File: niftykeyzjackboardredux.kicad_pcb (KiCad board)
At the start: 2 copper layers, 90 x 29.1 mm, 6 parts

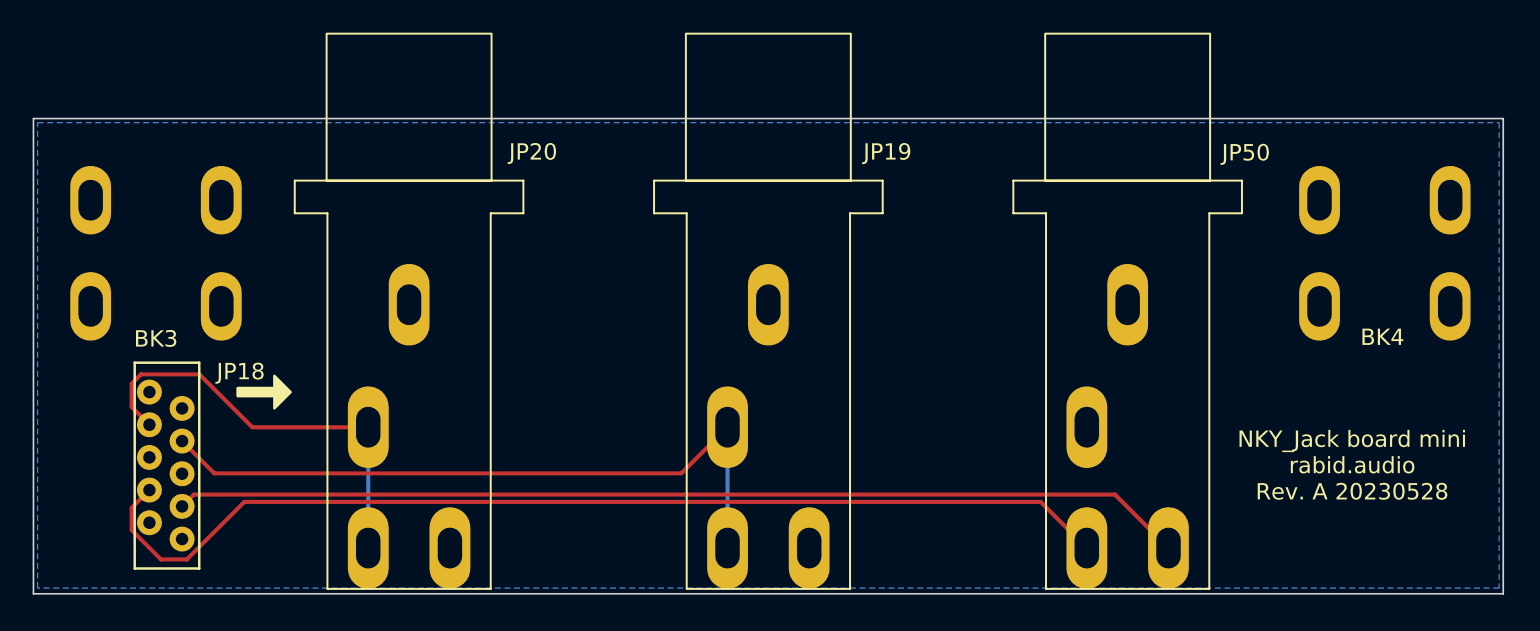
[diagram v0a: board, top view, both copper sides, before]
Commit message: adusted stick-out length
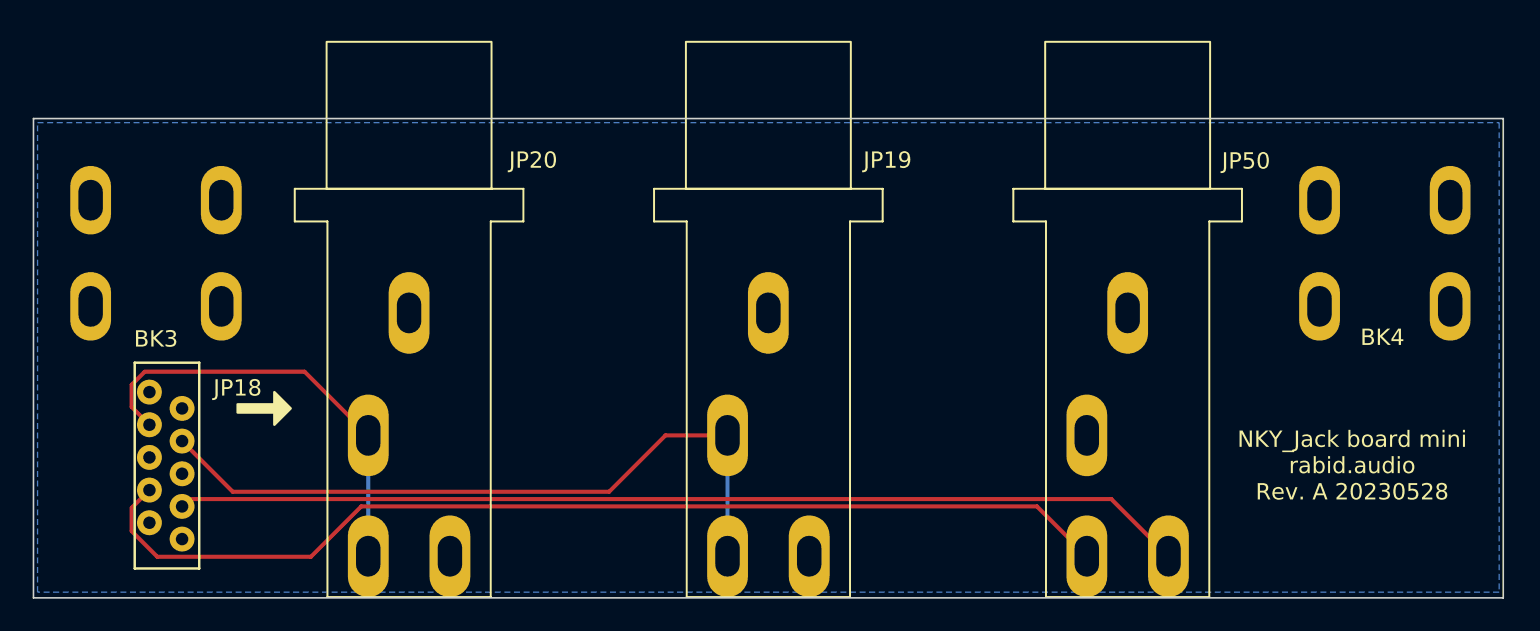
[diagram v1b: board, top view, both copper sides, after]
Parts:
- moved JP19 0.50 mm to (95.0, 67.0)
- moved JP20 0.50 mm to (73.0, 67.0)
- moved JP50 0.50 mm to (117.0, 67.0)
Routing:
- net Net-(JP19-PadT): track 42.8 -> 43.5 mm
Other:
- board size 90 x 29.1 mm -> 90 x 29.3 mm
- board text added: "(54.5-(3*10.6))/2 = 11.35 (54.5-10.6)/2=21.95 pushed jacks out extra 3.5mm from original"
- board text removed: "(54.5-(3*10.6))/2 = 11.35 (54.5-10.6)/2=21.95 pushed jacks out extra 4mm from original"
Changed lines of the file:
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@@
   )
   (footprint "components:Jack 6.35mm PJ603" locked (layer "F.Cu")
-    (at 117 66.5 -90)
+    (at 117 67 -90)
     (property "Sheetfile" "niftykeyzjackboardredux.kicad_sch")
     (property "Sheetname" "")
@@
       (effects (font (size 1 1) (thickness 0.15)))
     )
-    (fp_text value "HEADPHONES" (at -2.8 -3.5 -90) (layer "F.Fab")
+    (fp_text value "HEADPHONES" (at -2.8 -3.5 90) (layer "F.Fab")
       (effects (font (size 1 1) (thickness 0.15)))
     )
@@
   )
   (footprint "components:Jack 6.35mm PJ603" locked (layer "F.Cu")
-    (at 73 66.5 -90)
+    (at 73 67 -90)
     (property "Sheetfile" "niftykeyzjackboardredux.kicad_sch")
     (property "Sheetname" "")
@@
       (effects (font (size 1 1) (thickness 0.15)))
     )
-    (fp_text value "OUT1" (at -2.8 -3.5 -90) (layer "F.Fab")
+    (fp_text value "OUT1" (at -2.8 -3.5 90) (layer "F.Fab")
       (effects (font (size 1 1) (thickness 0.15)))
     )
@@
     (property "Sheetname" "")
     (attr through_hole)
-    (fp_text reference "JP18" (at 5.6 -1.25 unlocked) (layer "F.SilkS")
+    (fp_text reference "JP18" (at 5.4 -0.25 unlocked) (layer "F.SilkS")
       (effects (font (size 1 1) (thickness 0.15)))
     )
@@
       (effects (font (size 1 1) (thickness 0.15)))
     )
-    (fp_text user "${REFERENCE}" (at 5.6 -1.25 unlocked) (layer "F.Fab")
+    (fp_text user "${REFERENCE}" (at 5.4 -0.25 unlocked) (layer "F.Fab")
       (effects (font (size 1 1) (thickness 0.15)))
     )
@@
   )
   (footprint "components:Jack 6.35mm PJ603" locked (layer "F.Cu")
-    (at 95 66.5 -90)
+    (at 95 67 -90)
     (property "Sheetfile" "niftykeyzjackboardredux.kicad_sch")
     (property "Sheetname" "")
@@
       (effects (font (size 1 1) (thickness 0.15)))
     )
-    (fp_text value "OUT2" (at -2.8 -3.5 -90) (layer "F.Fab")
+    (fp_text value "OUT2" (at -2.8 -3.5 90) (layer "F.Fab")
       (effects (font (size 1 1) (thickness 0.15)))
     )
@@
   (gr_poly
     (pts
-      (xy 65.75 66.75)
-      (xy 64.75 67.75)
-      (xy 64.75 67)
-      (xy 62.5 67)
-      (xy 62.5 66.5)
-      (xy 64.75 66.5)
-      (xy 64.75 65.75)
+      (xy 65.75 67.75)
+      (xy 64.75 68.75)
+      (xy 64.75 68)
+      (xy 62.5 68)
+      (xy 62.5 67.5)
+      (xy 64.75 67.5)
+      (xy 64.75 66.75)
     ) (layer "F.SilkS") (width 0.15) (fill solid))
-  (gr_rect (start 50 50) (end 140 79.1) (layer "Edge.Cuts") (width 0.1) (fill none))
+  (gr_rect (start 50 50) (end 140 79.35) (layer "Edge.Cuts") (width 0.1) (fill none))
   (gr_text "NKY_Jack board mini\nrabid.audio\nRev. A 20230528" (at 130.75 71.25) (layer "F.SilkS")
     (effects (font (size 1 1) (thickness 0.15)))
   )
-  (gr_text "(54.5-(3*10.6))/2 = 11.35\n(54.5-10.6)/2=21.95\npushed jacks out extra 4mm from original" (at 80 38.75) (layer "F.Fab")
+  (gr_text "(54.5-(3*10.6))/2 = 11.35\n(54.5-10.6)/2=21.95\npushed jacks out extra 3.5mm from original" (at 80 38.75) (layer "F.Fab")
     (effects (font (size 1 1) (thickness 0.15)))
   )
-  (segment (start 59.825 73.025) (end 59.1 73.75) (width 0.25) (layer "F.Cu") (net 2))
-  (segment (start 116.225 73.025) (end 59.825 73.025) (width 0.25) (layer "F.Cu") (net 2))
-  (segment (start 119.5 76.3) (end 116.225 73.025) (width 0.25) (layer "F.Cu") (net 2))
-  (segment (start 60.163 65.663) (end 63.4 68.9) (width 0.25) (layer "F.Cu") (net 3))
-  (segment (start 56.013 67.663) (end 56.013 66.237) (width 0.25) (layer "F.Cu") (net 3))
+  (segment (start 119.5 76.8) (end 116 73.3) (width 0.25) (layer "F.Cu") (net 2))
+  (segment (start 116 73.3) (end 59.55 73.3) (width 0.25) (layer "F.Cu") (net 2))
+  (segment (start 59.55 73.3) (end 59.1 73.75) (width 0.25) (layer "F.Cu") (net 2))
+  (segment (start 56.013 66.299749) (end 56.812749 65.5) (width 0.25) (layer "F.Cu") (net 3))
+  (segment (start 56.013 67.663) (end 56.013 66.299749) (width 0.25) (layer "F.Cu") (net 3))
+  (segment (start 66.6 65.5) (end 70.5 69.4) (width 0.25) (layer "F.Cu") (net 3))
   (segment (start 57.1 68.75) (end 56.013 67.663) (width 0.25) (layer "F.Cu") (net 3))
-  (segment (start 56.013 66.237) (end 56.587 65.663) (width 0.25) (layer "F.Cu") (net 3))
-  (segment (start 56.587 65.663) (end 60.163 65.663) (width 0.25) (layer "F.Cu") (net 3))
-  (segment (start 63.4 68.9) (end 70.5 68.9) (width 0.25) (layer "F.Cu") (net 3))
-  (segment (start 70.5 68.9) (end 70.5 76.3) (width 0.25) (layer "B.Cu") (net 3))
-  (segment (start 89.675 71.725) (end 92.5 68.9) (width 0.25) (layer "F.Cu") (net 4))
-  (segment (start 59.1 69.75) (end 61.075 71.725) (width 0.25) (layer "F.Cu") (net 4))
-  (segment (start 61.075 71.725) (end 89.675 71.725) (width 0.25) (layer "F.Cu") (net 4))
-  (segment (start 92.5 68.9) (end 92.5 76.3) (width 0.25) (layer "B.Cu") (net 4))
-  (segment (start 56.013 73.837) (end 57.1 72.75) (width 0.25) (layer "F.Cu") (net 5))
-  (segment (start 62.912251 73.475) (end 59.387251 77) (width 0.25) (layer "F.Cu") (net 5))
-  (segment (start 57.812749 77) (end 56.013 75.200251) (width 0.25) (layer "F.Cu") (net 5))
-  (segment (start 59.387251 77) (end 57.812749 77) (width 0.25) (layer "F.Cu") (net 5))
-  (segment (start 111.675 73.475) (end 62.912251 73.475) (width 0.25) (layer "F.Cu") (net 5))
-  (segment (start 56.013 75.200251) (end 56.013 73.837) (width 0.25) (layer "F.Cu") (net 5))
-  (segment (start 114.5 76.3) (end 111.675 73.475) (width 0.25) (layer "F.Cu") (net 5))
+  (segment (start 56.812749 65.5) (end 66.6 65.5) (width 0.25) (layer "F.Cu") (net 3))
+  (segment (start 70.5 69.4) (end 70.5 76.8) (width 0.25) (layer "B.Cu") (net 3))
+  (segment (start 85.25 72.85) (end 88.7 69.4) (width 0.25) (layer "F.Cu") (net 4))
+  (segment (start 62.2 72.85) (end 85.25 72.85) (width 0.25) (layer "F.Cu") (net 4))
+  (segment (start 59.1 69.75) (end 62.2 72.85) (width 0.25) (layer "F.Cu") (net 4))
+  (segment (start 88.7 69.4) (end 92.5 69.4) (width 0.25) (layer "F.Cu") (net 4))
+  (segment (start 92.5 76.8) (end 92.5 69.4) (width 0.25) (layer "B.Cu") (net 4))
+  (segment (start 57.1 72.75) (end 56.013 73.837) (width 0.25) (layer "F.Cu") (net 5))
+  (segment (start 56.013 75.263) (end 57.587 76.837) (width 0.25) (layer "F.Cu") (net 5))
+  (segment (start 56.013 73.837) (end 56.013 75.263) (width 0.25) (layer "F.Cu") (net 5))
+  (segment (start 57.587 76.837) (end 66.985614 76.837) (width 0.25) (layer "F.Cu") (net 5))
+  (segment (start 70.072614 73.75) (end 111.45 73.75) (width 0.25) (layer "F.Cu") (net 5))
+  (segment (start 66.985614 76.837) (end 70.072614 73.75) (width 0.25) (layer "F.Cu") (net 5))
+  (segment (start 111.45 73.75) (end 114.5 76.8) (width 0.25) (layer "F.Cu") (net 5))
   (zone (net 1) (net_name "GND") (layer "B.Cu") (hatch edge 0.508)
     (connect_pads (clearance 0.508))
@@
     (polygon
       (pts
-        (xy 139.75 78.75)
-        (xy 50.25 78.75)
+        (xy 139.75 79)
+        (xy 50.25 79)
         (xy 50.25 50.25)
         (xy 139.75 50.25)
@@
     )
   )
+  (group "" locked (id 65ac9146-4b58-4e47-bd66-f6dcea7674e5)
+    (members
+      6b817d68-1e01-4d03-8519-fe86ffb6e69e
+      ba459322-174a-4526-8520-4337cc23d4d2
+      d0c782eb-eb72-43f2-9ef1-8a42a7ce99fa
+    )
+  )

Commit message: update board
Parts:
- moved BK3 0.64 mm to (53.5, 54.4)
- moved BK4 0.61 mm to (128.8, 54.4)
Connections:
- JP18 pad 3: Net-(JP20-PadT) -> Net-(JP18-Pad3)
- JP18 pad 4: Net-(JP19-PadT) -> Net-(JP18-Pad4)
- JP19 pad T: Net-(JP19-PadT) -> Net-(JP18-Pad4)
- JP19 pad TN: Net-(JP19-PadT) -> unconnected-(JP19-PadTN)
- JP20 pad T: Net-(JP20-PadT) -> Net-(JP18-Pad3)
- JP20 pad TN: Net-(JP20-PadT) -> unconnected-(JP20-PadTN)
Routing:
- net Net-(JP19-PadT): track 43.5 -> 0.00 mm
- net Net-(JP18-Pad4): track 0.00 -> 37.4 mm, vias 0 -> 1
- net Net-(JP20-PadT): track 26.7 -> 0.00 mm
- net Net-(JP18-Pad3): track 0.00 -> 23.4 mm
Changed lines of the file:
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@@
   (net 1 "GND")
   (net 2 "Net-(JP18-Pad8)")
-  (net 3 "Net-(JP20-PadT)")
-  (net 4 "Net-(JP19-PadT)")
-  (net 5 "Net-(JP50-PadT)")
+  (net 3 "Net-(JP18-Pad3)")
+  (net 4 "Net-(JP18-Pad4)")
+  (net 5 "Net-(JP18-Pad7)")
   (net 6 "unconnected-(JP50-PadTN)")
+  (net 7 "unconnected-(JP19-PadTN)")
+  (net 8 "unconnected-(JP20-PadTN)")
   (footprint "components:screw-mount" locked (layer "F.Cu")
-    (at 128.75 55)
+    (at 128.75 54.388)
     (property "Sheetfile" "niftykeyzjackboardredux.kicad_sch")
     (property "Sheetname" "")
@@
       (net 2 "Net-(JP18-Pad8)") (pintype "passive"))
     (pad "T" thru_hole oval locked (at 9.8 2.5 270) (size 5 2.5) (drill oval 2.5 1.5) (layers *.Cu *.Mask)
-      (net 5 "Net-(JP50-PadT)") (pintype "passive"))
+      (net 5 "Net-(JP18-Pad7)") (pintype "passive"))
     (pad "TN" thru_hole oval locked (at 2.4 2.5 270) (size 5 2.5) (drill oval 2.5 1.5) (layers *.Cu *.Mask)
       (net 6 "unconnected-(JP50-PadTN)") (pintype "passive+no_connect"))
   )
   (footprint "components:screw-mount" locked (layer "F.Cu")
-    (at 53.5 55)
+    (at 53.5 54.356)
     (property "Sheetfile" "niftykeyzjackboardredux.kicad_sch")
     (property "Sheetname" "")
@@
       (net 1 "GND") (pintype "passive"))
     (pad "T" thru_hole oval locked (at 9.8 2.5 270) (size 5 2.5) (drill oval 2.5 1.5) (layers *.Cu *.Mask)
-      (net 3 "Net-(JP20-PadT)") (pintype "passive"))
+      (net 3 "Net-(JP18-Pad3)") (pintype "passive"))
     (pad "TN" thru_hole oval locked (at 2.4 2.5 270) (size 5 2.5) (drill oval 2.5 1.5) (layers *.Cu *.Mask)
-      (net 3 "Net-(JP20-PadT)") (pintype "passive"))
+      (net 8 "unconnected-(JP20-PadTN)") (pintype "passive+no_connect"))
   )
   (footprint "components:HLW10S-2C7LF" (layer "F.Cu")
@@
       (net 1 "GND") (pinfunction "Pin_2") (pintype "passive"))
     (pad "3" thru_hole circle (at 0 2) (size 1.524 1.524) (drill 0.762) (layers *.Cu *.Mask)
-      (net 3 "Net-(JP20-PadT)") (pinfunction "Pin_3") (pintype "passive"))
+      (net 3 "Net-(JP18-Pad3)") (pinfunction "Pin_3") (pintype "passive"))
     (pad "4" thru_hole circle (at 2 3) (size 1.524 1.524) (drill 0.762) (layers *.Cu *.Mask)
-      (net 4 "Net-(JP19-PadT)") (pinfunction "Pin_4") (pintype "passive"))
+      (net 4 "Net-(JP18-Pad4)") (pinfunction "Pin_4") (pintype "passive"))
     (pad "5" thru_hole circle (at 0 4) (size 1.524 1.524) (drill 0.762) (layers *.Cu *.Mask)
       (net 1 "GND") (pinfunction "Pin_5") (pintype "passive"))
@@
       (net 1 "GND") (pinfunction "Pin_6") (pintype "passive"))
     (pad "7" thru_hole circle (at 0 6) (size 1.524 1.524) (drill 0.762) (layers *.Cu *.Mask)
-      (net 5 "Net-(JP50-PadT)") (pinfunction "Pin_7") (pintype "passive"))
+      (net 5 "Net-(JP18-Pad7)") (pinfunction "Pin_7") (pintype "passive"))
     (pad "8" thru_hole circle (at 2 7) (size 1.524 1.524) (drill 0.762) (layers *.Cu *.Mask)
       (net 2 "Net-(JP18-Pad8)") (pinfunction "Pin_8") (pintype "passive"))
@@
       (net 1 "GND") (pintype "passive"))
     (pad "T" thru_hole oval locked (at 9.8 2.5 270) (size 5 2.5) (drill oval 2.5 1.5) (layers *.Cu *.Mask)
-      (net 4 "Net-(JP19-PadT)") (pintype "passive"))
+      (net 4 "Net-(JP18-Pad4)") (pintype "passive"))
     (pad "TN" thru_hole oval locked (at 2.4 2.5 270) (size 5 2.5) (drill oval 2.5 1.5) (layers *.Cu *.Mask)
-      (net 4 "Net-(JP19-PadT)") (pintype "passive"))
+      (net 7 "unconnected-(JP19-PadTN)") (pintype "passive+no_connect"))
   )
   (gr_rect (start 60.15 64.95) (end 56.2 77.55) (layer "F.SilkS") (width 0.15) (fill none))
@@
   (segment (start 116 73.3) (end 59.55 73.3) (width 0.25) (layer "F.Cu") (net 2))
   (segment (start 59.55 73.3) (end 59.1 73.75) (width 0.25) (layer "F.Cu") (net 2))
-  (segment (start 56.013 66.299749) (end 56.812749 65.5) (width 0.25) (layer "F.Cu") (net 3))
-  (segment (start 56.013 67.663) (end 56.013 66.299749) (width 0.25) (layer "F.Cu") (net 3))
-  (segment (start 66.6 65.5) (end 70.5 69.4) (width 0.25) (layer "F.Cu") (net 3))
-  (segment (start 57.1 68.75) (end 56.013 67.663) (width 0.25) (layer "F.Cu") (net 3))
-  (segment (start 56.812749 65.5) (end 66.6 65.5) (width 0.25) (layer "F.Cu") (net 3))
-  (segment (start 70.5 69.4) (end 70.5 76.8) (width 0.25) (layer "B.Cu") (net 3))
-  (segment (start 85.25 72.85) (end 88.7 69.4) (width 0.25) (layer "F.Cu") (net 4))
+  (segment (start 55.563 70.287) (end 55.563 75.449396) (width 0.25) (layer "F.Cu") (net 3))
+  (segment (start 69.83 77.47) (end 70.5 76.8) (width 0.25) (layer "F.Cu") (net 3))
+  (segment (start 55.563 75.449396) (end 57.583604 77.47) (width 0.25) (layer "F.Cu") (net 3))
+  (segment (start 57.1 68.75) (end 55.563 70.287) (width 0.25) (layer "F.Cu") (net 3))
+  (segment (start 57.583604 77.47) (end 69.83 77.47) (width 0.25) (layer "F.Cu") (net 3))
   (segment (start 62.2 72.85) (end 85.25 72.85) (width 0.25) (layer "F.Cu") (net 4))
   (segment (start 59.1 69.75) (end 62.2 72.85) (width 0.25) (layer "F.Cu") (net 4))
-  (segment (start 88.7 69.4) (end 92.5 69.4) (width 0.25) (layer "F.Cu") (net 4))
-  (segment (start 92.5 76.8) (end 92.5 69.4) (width 0.25) (layer "B.Cu") (net 4))
+  (segment (start 86.36 71.74) (end 86.36 71.628) (width 0.25) (layer "F.Cu") (net 4))
+  (segment (start 85.25 72.85) (end 86.36 71.74) (width 0.25) (layer "F.Cu") (net 4))
+  (via (at 86.36 71.628) (size 0.8) (drill 0.4) (layers "F.Cu" "B.Cu") (net 4))
+  (segment (start 91.532 76.8) (end 92.5 76.8) (width 0.25) (layer "B.Cu") (net 4))
+  (segment (start 86.36 71.628) (end 91.532 76.8) (width 0.25) (layer "B.Cu") (net 4))
   (segment (start 57.1 72.75) (end 56.013 73.837) (width 0.25) (layer "F.Cu") (net 5))
   (segment (start 56.013 75.263) (end 57.587 76.837) (width 0.25) (layer "F.Cu") (net 5))
